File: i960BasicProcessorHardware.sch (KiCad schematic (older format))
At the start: 66 parts, among them J1 Conn_02x16_Odd_Even, J10 Conn_01x03, J11 Conn_01x08, J2 Conn_02x39_Odd_Even, J3 Conn_01x03, J4 Conn_02x05_Odd_Even, J5 Conn_02x05_Odd_Even, J6 Conn_02x05_Odd_Even, J7 Conn_01x06, J9 Conn_01x11, U1 74HC245, U10 74LS08, U11 74LS04, U12 74LS174, U13 SN74LVC245AN, U14 74LS174, U15 MCP23S17_SP, U16 MCP23S17_SP, U17 MCP23S17_SP, U2 80960Sx, U3 MCP23S17_SP, U4 74HC245, U5 74HC573, U6 74HC573, U7 Adafruit_FeatherWing (PSRAM F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, U8 Adafruit_FeatherWing (PSRAM F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, U9 74LS125

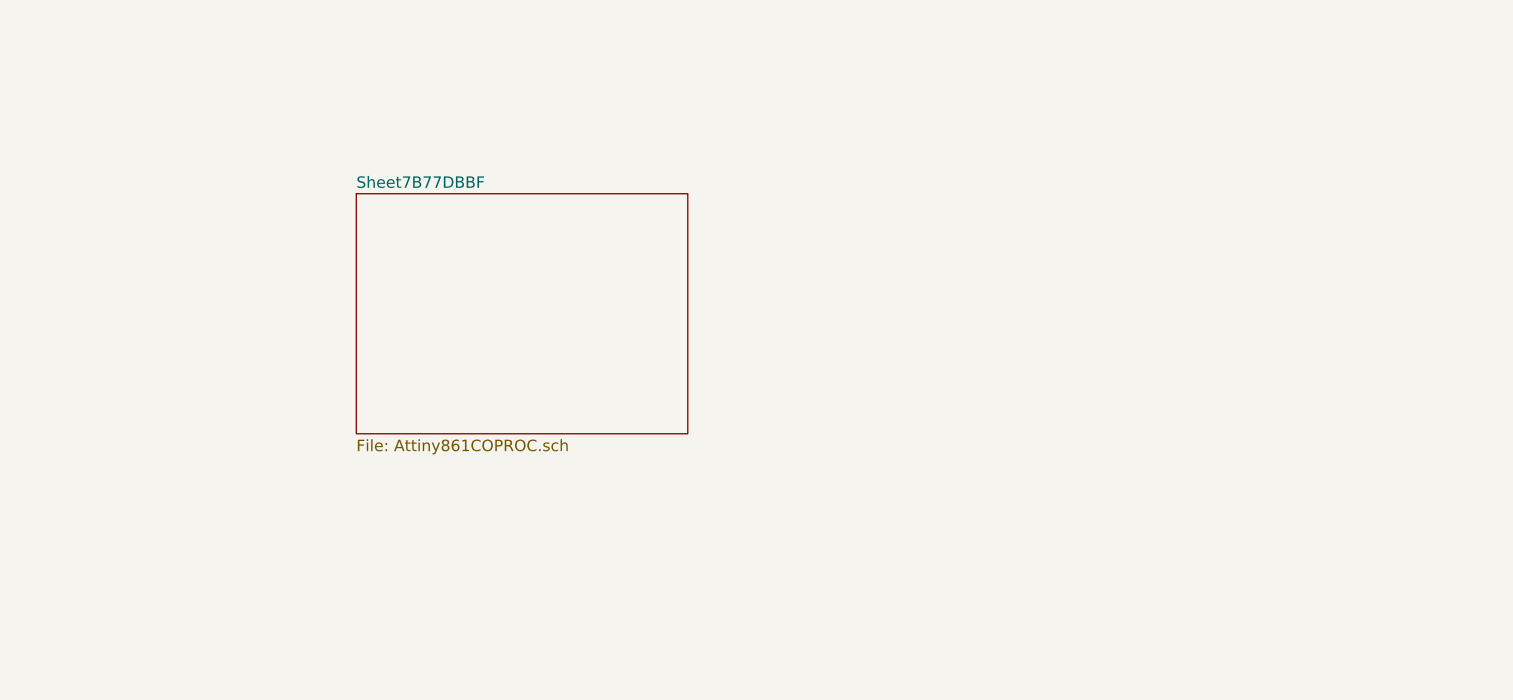
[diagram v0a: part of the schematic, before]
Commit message: fixup int0 for the attiny861 to be pb6
Add a second attiny861
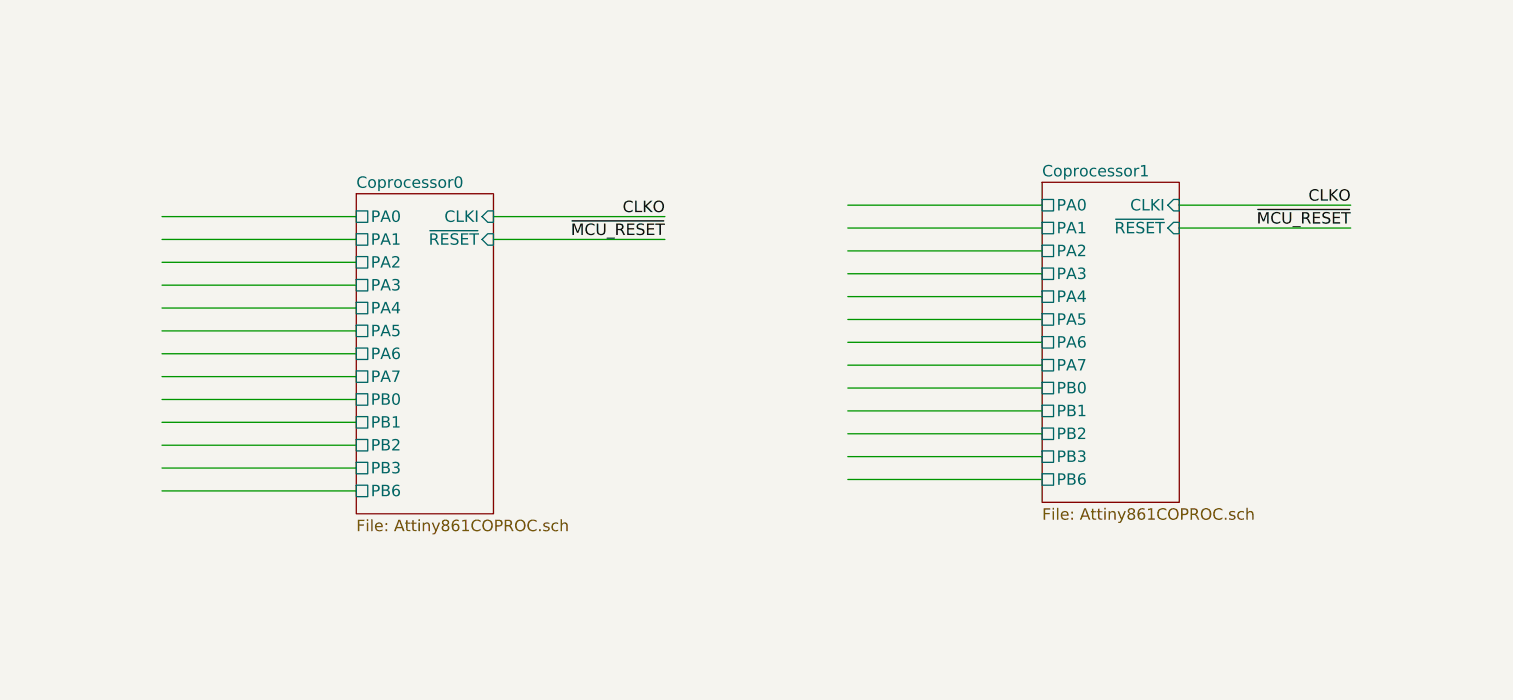
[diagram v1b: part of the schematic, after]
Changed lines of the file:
@@
 $EndComp
 $Sheet
-S 14100 1250 1450 1050
+S 14100 1250 600  1400
 U 7B77DBC0
-F0 "Sheet7B77DBBF" 50
+F0 "Coprocessor0" 50
 F1 "Attiny861COPROC.sch" 50
+F2 "CLKI" I R 14700 1350 50
+F3 "PB6" U L 14100 2550 50
+F4 "~RESET" I R 14700 1450 50
+F5 "PA0" U L 14100 1350 50
+F6 "PA1" U L 14100 1450 50
+F7 "PA2" U L 14100 1550 50
+F8 "PA3" U L 14100 1650 50
+F9 "PA4" U L 14100 1750 50
+F10 "PA5" U L 14100 1850 50
+F11 "PA6" U L 14100 1950 50
+F12 "PA7" U L 14100 2050 50
+F13 "PB0" U L 14100 2150 50
+F14 "PB1" U L 14100 2250 50
+F15 "PB2" U L 14100 2350 50
+F16 "PB3" U L 14100 2450 50
 $EndSheet
+Wire Wire Line
+	14700 1350 15450 1350
+Wire Wire Line
+	14700 1450 15450 1450
+Text Label 15450 1350 2    50   ~ 0
+CLKO
+Text Label 15450 1450 2    50   ~ 0
+~MCU_RESET
+Wire Wire Line
+	14100 1350 13250 1350
+Wire Wire Line
+	14100 1450 13250 1450
+Wire Wire Line
+	14100 1550 13250 1550
+Wire Wire Line
+	14100 1650 13250 1650
+Wire Wire Line
+	14100 1750 13250 1750
+Wire Wire Line
+	14100 1850 13250 1850
+Wire Wire Line
+	14100 1950 13250 1950
+Wire Wire Line
+	14100 2050 13250 2050
+Wire Wire Line
+	14100 2150 13250 2150
+Wire Wire Line
+	14100 2250 13250 2250
+Wire Wire Line
+	14100 2350 13250 2350
+Wire Wire Line
+	14100 2450 13250 2450
+Wire Wire Line
+	13250 2550 14100 2550
+$Sheet
+S 17100 1200 600  1400
+U 7C66C7D3
+F0 "Coprocessor1" 50
+F1 "Attiny861COPROC.sch" 50
+F2 "CLKI" I R 17700 1300 50
+F3 "PB6" U L 17100 2500 50
+F4 "~RESET" I R 17700 1400 50
+F5 "PA0" U L 17100 1300 50
+F6 "PA1" U L 17100 1400 50
+F7 "PA2" U L 17100 1500 50
+F8 "PA3" U L 17100 1600 50
+F9 "PA4" U L 17100 1700 50
+F10 "PA5" U L 17100 1800 50
+F11 "PA6" U L 17100 1900 50
+F12 "PA7" U L 17100 2000 50
+F13 "PB0" U L 17100 2100 50
+F14 "PB1" U L 17100 2200 50
+F15 "PB2" U L 17100 2300 50
+F16 "PB3" U L 17100 2400 50
+$EndSheet
+Wire Wire Line
+	17700 1300 18450 1300
+Wire Wire Line
+	17700 1400 18450 1400
+Text Label 18450 1300 2    50   ~ 0
+CLKO
+Text Label 18450 1400 2    50   ~ 0
+~MCU_RESET
+Wire Wire Line
+	17100 1300 16250 1300
+Wire Wire Line
+	17100 1400 16250 1400
+Wire Wire Line
+	17100 1500 16250 1500
+Wire Wire Line
+	17100 1600 16250 1600
+Wire Wire Line
+	17100 1700 16250 1700
+Wire Wire Line
+	17100 1800 16250 1800
+Wire Wire Line
+	17100 1900 16250 1900
+Wire Wire Line
+	17100 2000 16250 2000
+Wire Wire Line
+	17100 2100 16250 2100
+Wire Wire Line
+	17100 2200 16250 2200
+Wire Wire Line
+	17100 2300 16250 2300
+Wire Wire Line
+	17100 2400 16250 2400
+Wire Wire Line
+	16250 2500 17100 2500
 $EndSCHEMATC

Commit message: We always have access to the 861s
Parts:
- renumbered C24 to C14, C14 to C15, C15 to C16, C16 to C17, C17 to C18, C25 to C19, C26 to C20, C18 to C21, C19 to C22, C20 to C23, C21 to C24, C22 to C25, C23 to C26, D2 to D1, J11 to J1, J3 to J10, J10 to J11, J7 to J12, J9 to J13, J2 to J14, J1 to J9, R4 to R2, R2 to R3, R3 to R4, U7 to U10, U8 to U11, U9 to U12, U11 to U13, U10 to U14, U12 to U15, U13 to U16, U14 to U17, U15 to U3, U3 to U4, U4 to U5, U5 to U6, U6 to U7, U16 to U8, U17 to U9
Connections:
- net ~RESET85: no longer names the net of RN1.6 (R5)
- no-connect marks 85 -> 86

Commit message: pull in a 1284p socket setup
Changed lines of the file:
@@
 $Descr A1 33110 23386
 encoding utf-8
-Sheet 1 3
+Sheet 1 4
 Title "i960Sx Basic Processor Hardware Board"
 Date "2021-10-16"
@@
 	1    0    0    -1
 $EndComp
-$Sheet
-S 14100 1250 600  1400
-U 7B77DBC0
-F0 "Coprocessor0" 50
-F1 "Attiny861COPROC.sch" 50
-F2 "CLKI" I R 14700 1350 50
-F3 "PB6" U L 14100 2550 50
-F4 "~RESET" I R 14700 1450 50
-F5 "PA0" U L 14100 1350 50
-F6 "PA1" U L 14100 1450 50
-F7 "PA2" U L 14100 1550 50
-F8 "PA3" U L 14100 1650 50
-F9 "PA4" U L 14100 1750 50
-F10 "PA5" U L 14100 1850 50
-F11 "PA6" U L 14100 1950 50
-F12 "PA7" U L 14100 2050 50
-F13 "PB0" U L 14100 2150 50
-F14 "PB1" U L 14100 2250 50
-F15 "PB2" U L 14100 2350 50
-F16 "PB3" U L 14100 2450 50
-$EndSheet
+NoConn ~ 27900 21350
 Wire Wire Line
-	14700 1350 15450 1350
+	14100 2550 13250 2550
 Wire Wire Line
-	14700 1450 15450 1450
-Text Label 15450 1350 2    50   ~ 0
-CLKO
-Text Label 15450 1450 2    50   ~ 0
-~MCU_RESET
+	14100 2450 13250 2450
 Wire Wire Line
-	17700 1300 18450 1300
+	14100 2350 13250 2350
 Wire Wire Line
-	17700 1400 18450 1400
-Text Label 18450 1300 2    50   ~ 0
-CLKO
-Text Label 18450 1400 2    50   ~ 0
-~MCU_RESET
+	14100 2250 13250 2250
 Wire Wire Line
-	17100 1300 16250 1300
+	14100 2150 13250 2150
 Wire Wire Line
-	17100 1400 16250 1400
+	14100 2050 13250 2050
 Wire Wire Line
-	17100 1500 16250 1500
+	14100 1950 13250 1950
 Wire Wire Line
-	17100 1600 16250 1600
+	14100 1850 13250 1850
 Wire Wire Line
-	17100 1700 16250 1700
+	14100 1750 13250 1750
 Wire Wire Line
-	17100 1800 16250 1800
+	14100 1650 13250 1650
 Wire Wire Line
-	17100 1900 16250 1900
+	14100 1550 13250 1550
 Wire Wire Line
-	17100 2000 16250 2000
+	14100 1450 13250 1450
+Wire Wire Line
+	14100 1350 13250 1350
+Wire Wire Line
+	17100 2500 16250 2500
+Wire Wire Line
+	17100 2400 16250 2400
+Wire Wire Line
+	17100 2300 16250 2300
+Wire Wire Line
+	17100 2200 16250 2200
+Wire Wire Line
+	17100 2100 16250 2100
 $Sheet
 S 17100 1200 600  1400
@@
 F16 "PB3" U L 17100 2400 50
 $EndSheet
-NoConn ~ 27900 21350
 Wire Wire Line
-	17100 2100 16250 2100
-Wire Wire Line
-	17100 2200 16250 2200
-Wire Wire Line
-	17100 2300 16250 2300
-Wire Wire Line
-	17100 2400 16250 2400
-Wire Wire Line
-	17100 2500 16250 2500
-Wire Wire Line
-	14100 1350 13250 1350
-Wire Wire Line
-	14100 1450 13250 1450
+	17100 2000 16250 2000
 Wire Wire Line
-	14100 1550 13250 1550
+	17100 1900 16250 1900
 Wire Wire Line
-	14100 1650 13250 1650
+	17100 1800 16250 1800
 Wire Wire Line
-	14100 1750 13250 1750
+	17100 1700 16250 1700
 Wire Wire Line
-	14100 1850 13250 1850
+	17100 1600 16250 1600
 Wire Wire Line
-	14100 1950 13250 1950
+	17100 1500 16250 1500
 Wire Wire Line
-	14100 2050 13250 2050
+	17100 1400 16250 1400
 Wire Wire Line
-	14100 2150 13250 2150
+	17100 1300 16250 1300
+Text Label 18450 1400 2    50   ~ 0
+~MCU_RESET
+Text Label 18450 1300 2    50   ~ 0
+CLKO
 Wire Wire Line
-	14100 2250 13250 2250
+	17700 1400 18450 1400
 Wire Wire Line
-	14100 2350 13250 2350
+	17700 1300 18450 1300
+Text Label 15450 1450 2    50   ~ 0
+~MCU_RESET
+Text Label 15450 1350 2    50   ~ 0
+CLKO
 Wire Wire Line
-	14100 2450 13250 2450
+	14700 1450 15450 1450
 Wire Wire Line
-	14100 2550 13250 2550
+	14700 1350 15450 1350
+$Sheet
+S 14100 1250 600  1400
+U 7B77DBC0
+F0 "Coprocessor0" 50
+F1 "Attiny861COPROC.sch" 50
+F2 "CLKI" I R 14700 1350 50
+F3 "PB6" U L 14100 2550 50
+F4 "~RESET" I R 14700 1450 50
+F5 "PA0" U L 14100 1350 50
+F6 "PA1" U L 14100 1450 50
+F7 "PA2" U L 14100 1550 50
+F8 "PA3" U L 14100 1650 50
+F9 "PA4" U L 14100 1750 50
+F10 "PA5" U L 14100 1850 50
+F11 "PA6" U L 14100 1950 50
+F12 "PA7" U L 14100 2050 50
+F13 "PB0" U L 14100 2150 50
+F14 "PB1" U L 14100 2250 50
+F15 "PB2" U L 14100 2350 50
+F16 "PB3" U L 14100 2450 50
+$EndSheet
+$Sheet
+S 20200 2300 1800 2350
+U 7D8CCC7A
+F0 "Sheet7D8CCC79" 50
+F1 "ATMEGAx4SeriesCoprocessor.sch" 50
+$EndSheet
 $EndSCHEMATC

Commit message: Drop the attiny861s and add the 1284p based coprocessor in its place
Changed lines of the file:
@@
 $Descr A1 33110 23386
 encoding utf-8
-Sheet 1 4
+Sheet 1 2
 Title "i960Sx Basic Processor Hardware Board"
 Date "2021-10-16"
@@
 $EndComp
 NoConn ~ 27900 21350
-Wire Wire Line
-	14100 2550 13250 2550
-Wire Wire Line
-	14100 2450 13250 2450
-Wire Wire Line
-	14100 2350 13250 2350
-Wire Wire Line
-	14100 2250 13250 2250
-Wire Wire Line
-	14100 2150 13250 2150
-Wire Wire Line
-	14100 2050 13250 2050
-Wire Wire Line
-	14100 1950 13250 1950
-Wire Wire Line
-	14100 1850 13250 1850
-Wire Wire Line
-	14100 1750 13250 1750
-Wire Wire Line
-	14100 1650 13250 1650
-Wire Wire Line
-	14100 1550 13250 1550
-Wire Wire Line
-	14100 1450 13250 1450
-Wire Wire Line
-	14100 1350 13250 1350
-Wire Wire Line
-	17100 2500 16250 2500
-Wire Wire Line
-	17100 2400 16250 2400
-Wire Wire Line
-	17100 2300 16250 2300
-Wire Wire Line
-	17100 2200 16250 2200
-Wire Wire Line
-	17100 2100 16250 2100
-$Sheet
-S 17100 1200 600  1400
-U 7C66C7D3
-F0 "Coprocessor1" 50
-F1 "Attiny861COPROC.sch" 50
-F2 "CLKI" I R 17700 1300 50
-F3 "PB6" U L 17100 2500 50
-F4 "~RESET" I R 17700 1400 50
-F5 "PA0" U L 17100 1300 50
-F6 "PA1" U L 17100 1400 50
-F7 "PA2" U L 17100 1500 50
-F8 "PA3" U L 17100 1600 50
-F9 "PA4" U L 17100 1700 50
-F10 "PA5" U L 17100 1800 50
-F11 "PA6" U L 17100 1900 50
-F12 "PA7" U L 17100 2000 50
-F13 "PB0" U L 17100 2100 50
-F14 "PB1" U L 17100 2200 50
-F15 "PB2" U L 17100 2300 50
-F16 "PB3" U L 17100 2400 50
-$EndSheet
-Wire Wire Line
-	17100 2000 16250 2000
-Wire Wire Line
-	17100 1900 16250 1900
-Wire Wire Line
-	17100 1800 16250 1800
-Wire Wire Line
-	17100 1700 16250 1700
-Wire Wire Line
-	17100 1600 16250 1600
-Wire Wire Line
-	17100 1500 16250 1500
-Wire Wire Line
-	17100 1400 16250 1400
-Wire Wire Line
-	17100 1300 16250 1300
-Text Label 18450 1400 2    50   ~ 0
-~MCU_RESET
-Text Label 18450 1300 2    50   ~ 0
-CLKO
-Wire Wire Line
-	17700 1400 18450 1400
-Wire Wire Line
-	17700 1300 18450 1300
-Text Label 15450 1450 2    50   ~ 0
-~MCU_RESET
-Text Label 15450 1350 2    50   ~ 0
-CLKO
-Wire Wire Line
-	14700 1450 15450 1450
-Wire Wire Line
-	14700 1350 15450 1350
-$Sheet
-S 14100 1250 600  1400
-U 7B77DBC0
-F0 "Coprocessor0" 50
-F1 "Attiny861COPROC.sch" 50
-F2 "CLKI" I R 14700 1350 50
-F3 "PB6" U L 14100 2550 50
-F4 "~RESET" I R 14700 1450 50
-F5 "PA0" U L 14100 1350 50
-F6 "PA1" U L 14100 1450 50
-F7 "PA2" U L 14100 1550 50
-F8 "PA3" U L 14100 1650 50
-F9 "PA4" U L 14100 1750 50
-F10 "PA5" U L 14100 1850 50
-F11 "PA6" U L 14100 1950 50
-F12 "PA7" U L 14100 2050 50
-F13 "PB0" U L 14100 2150 50
-F14 "PB1" U L 14100 2250 50
-F15 "PB2" U L 14100 2350 50
-F16 "PB3" U L 14100 2450 50
-$EndSheet
 $Sheet
 S 20200 2300 1800 2350

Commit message: ATMEGAx4 coprocessor is basically setup
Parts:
- renumbered J14 to J10, J4 to J2, J5 to J3, J6 to J4, J9 to J5, J10 to J6, J11 to J7, J12 to J8, J13 to J9
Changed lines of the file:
@@
 DT\~R
 $Comp
-L Connector_Generic:Conn_02x39_Odd_Even J14
+L Connector_Generic:Conn_02x39_Odd_Even J10
 U 1 1 6A3C2242
 P 30100 2650
-F 0 "J14" H 30150 4767 50  0000 C CNN
+F 0 "J10" H 30150 4767 50  0000 C CNN
 F 1 "Conn_02x39_Odd_Even" H 30150 4676 50  0000 C CNN
 F 2 "Connector_PinHeader_2.54mm:PinHeader_2x39_P2.54mm_Vertical" H 30100 2650 50  0001 C CNN
@@
 $EndComp
 $Comp
-L Connector_Generic:Conn_02x05_Odd_Even J4
+L Connector_Generic:Conn_02x05_Odd_Even J2
 U 1 1 74368C12
 P 13750 4400
-F 0 "J4" H 13800 4817 50  0000 C CNN
+F 0 "J2" H 13800 4817 50  0000 C CNN
 F 1 "Conn_02x05_Odd_Even" H 13800 4726 50  0000 C CNN
 F 2 "Connector_PinHeader_2.54mm:PinHeader_2x05_P2.54mm_Vertical" H 13750 4400 50  0001 C CNN
@@
 $EndComp
 $Comp
-L Connector_Generic:Conn_02x05_Odd_Even J5
+L Connector_Generic:Conn_02x05_Odd_Even J3
 U 1 1 744AC6A7
 P 13750 6200
-F 0 "J5" H 13800 6617 50  0000 C CNN
+F 0 "J3" H 13800 6617 50  0000 C CNN
 F 1 "Conn_02x05_Odd_Even" H 13800 6526 50  0000 C CNN
 F 2 "Connector_PinHeader_2.54mm:PinHeader_2x05_P2.54mm_Vertical" H 13750 6200 50  0001 C CNN
@@
 $EndComp
 $Comp
-L Connector_Generic:Conn_02x05_Odd_Even J6
+L Connector_Generic:Conn_02x05_Odd_Even J4
 U 1 1 745F5BFF
 P 15150 6050
-F 0 "J6" H 15200 6467 50  0000 C CNN
+F 0 "J4" H 15200 6467 50  0000 C CNN
 F 1 "Conn_02x05_Odd_Even" H 15200 6376 50  0000 C CNN
 F 2 "Connector_PinHeader_2.54mm:PinHeader_2x05_P2.54mm_Vertical" H 15150 6050 50  0001 C CNN
@@
 $EndComp
 $Comp
-L Connector_Generic:Conn_01x06 J12
+L Connector_Generic:Conn_01x06 J8
 U 1 1 74743549
 P 17900 5000
-F 0 "J12" H 17980 4992 50  0000 L CNN
+F 0 "J8" H 17980 4992 50  0000 L CNN
 F 1 "Conn_01x06" H 17980 4901 50  0000 L CNN
 F 2 "Connector_PinHeader_2.54mm:PinHeader_1x06_P2.54mm_Vertical" H 17900 5000 50  0001 C CNN
@@
 ~INT0
 $Comp
-L Connector_Generic:Conn_01x03 J10
+L Connector_Generic:Conn_01x03 J6
 U 1 1 769276F2
 P 17000 17900
-F 0 "J10" H 17080 17942 50  0000 L CNN
+F 0 "J6" H 17080 17942 50  0000 L CNN
 F 1 "Conn_01x03" H 17080 17851 50  0000 L CNN
 F 2 "Connector_PinHeader_2.54mm:PinHeader_1x03_P2.54mm_Vertical" H 17000 17900 50  0001 C CNN
@@
 NoConn ~ 12050 16300
 $Comp
-L Connector_Generic:Conn_01x03 J11
+L Connector_Generic:Conn_01x03 J7
 U 1 1 780859B4
 P 17000 18900
-F 0 "J11" H 17080 18942 50  0000 L CNN
+F 0 "J7" H 17080 18942 50  0000 L CNN
 F 1 "Conn_01x03" H 17080 18851 50  0000 L CNN
 F 2 "Connector_PinHeader_2.54mm:PinHeader_1x03_P2.54mm_Vertical" H 17000 18900 50  0001 C CNN
@@
 GPB7
 $Comp
-L Connector_Generic:Conn_02x16_Odd_Even J9
+L Connector_Generic:Conn_02x16_Odd_Even J5
 U 1 1 79DF032E
 P 17000 16500
-F 0 "J9" H 17050 17417 50  0000 C CNN
+F 0 "J5" H 17050 17417 50  0000 C CNN
 F 1 "Conn_02x16_Odd_Even" H 17050 17326 50  0000 C CNN
 F 2 "Connector_PinHeader_2.54mm:PinHeader_2x16_P2.54mm_Vertical" H 17000 16500 50  0001 C CNN
@@
 GPB7
 $Comp
-L Connector_Generic:Conn_01x11 J13
+L Connector_Generic:Conn_01x11 J9
 U 1 1 79F7F59B
 P 19400 17500
-F 0 "J13" H 19480 17542 50  0000 L CNN
+F 0 "J9" H 19480 17542 50  0000 L CNN
 F 1 "Conn_01x11" H 19480 17451 50  0000 L CNN
 F 2 "Connector_PinHeader_2.54mm:PinHeader_1x11_P2.54mm_Vertical" H 19400 17500 50  0001 C CNN
